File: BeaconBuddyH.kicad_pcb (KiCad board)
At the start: 2 copper layers, 25.4 x 27.9 mm, 106 parts, among them P1 CONN_01X06, U1 nRF52832-QFAA, Y1 32.768kHz, Y2 32MHz

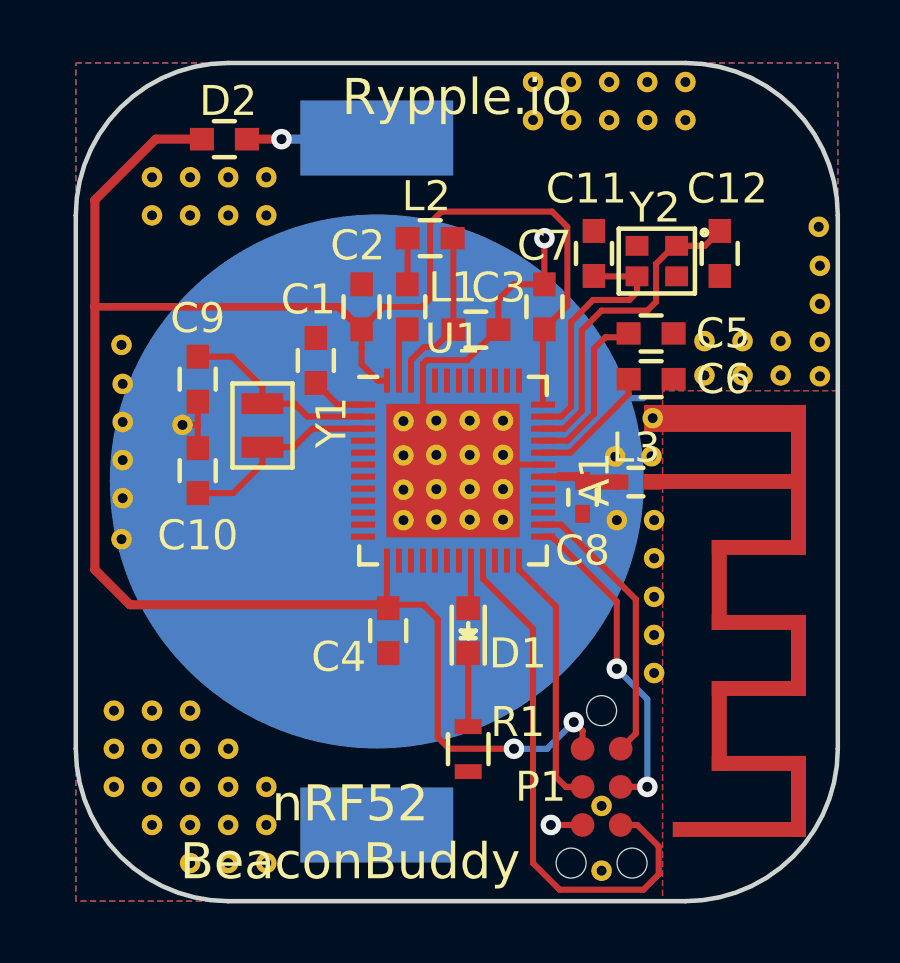
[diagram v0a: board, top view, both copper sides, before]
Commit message: Added Temp/Humidity sensor
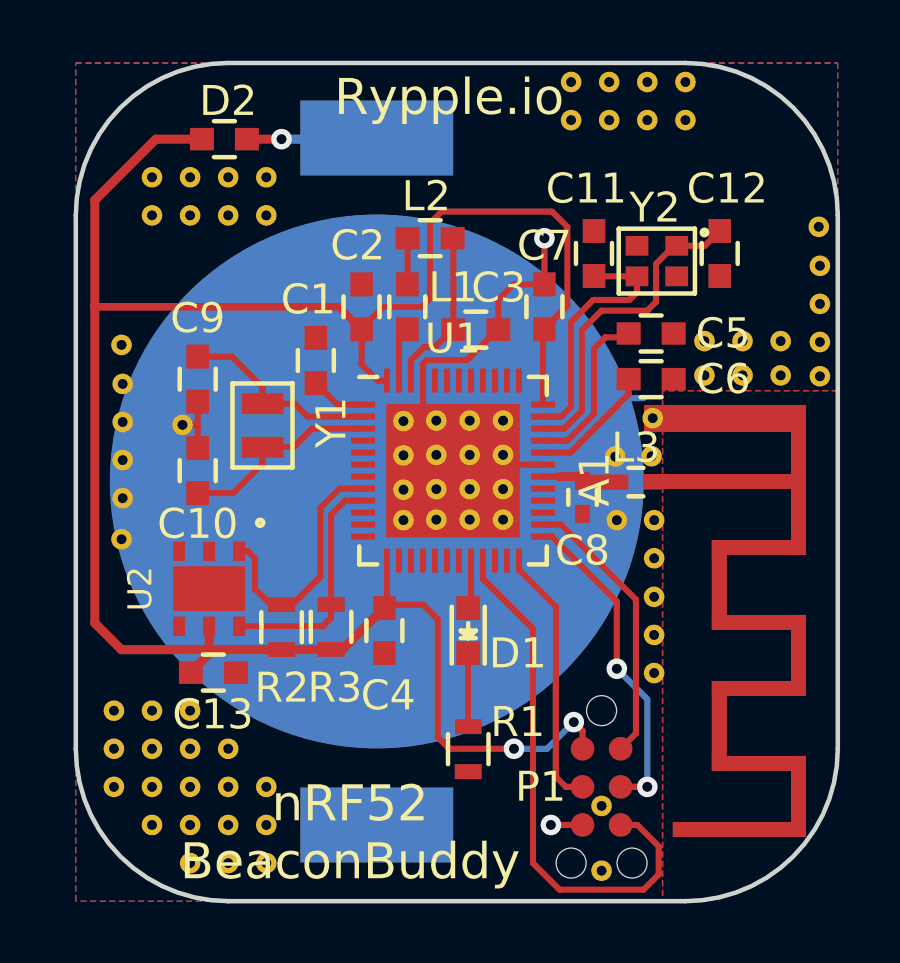
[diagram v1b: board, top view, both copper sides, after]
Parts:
- removed the REF**11 at (167.6, 102.2)
- removed the REF**12 at (167.6, 101.0)
- added C13: 0.1uF, Capacitors_SMD:C_0603, F.Cu at (157.0, 120.7)
- added R2: 470, Resistors_SMD:R_0603, F.Cu at (159.3, 119.1)
- added R3: 470, Resistors_SMD:R_0603, F.Cu at (160.9, 119.1)
- added U2: HDC1080, New_Footprints:S-PWSON-N6, F.Cu at (156.8, 117.9)
- moved C4 0.13 mm to (162.7, 119.3)
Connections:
- U1 pad 8: Net-(U1-Pad8) -> /SDA
- U1 pad 9: Net-(U1-Pad9) -> /SCL
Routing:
- net /SDA: track 0.00 -> 8.40 mm
- net /SCL: track 0.00 -> 7.88 mm
- net VDD: track 68.6 -> 73.1 mm

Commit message: Added Pressure Sensor
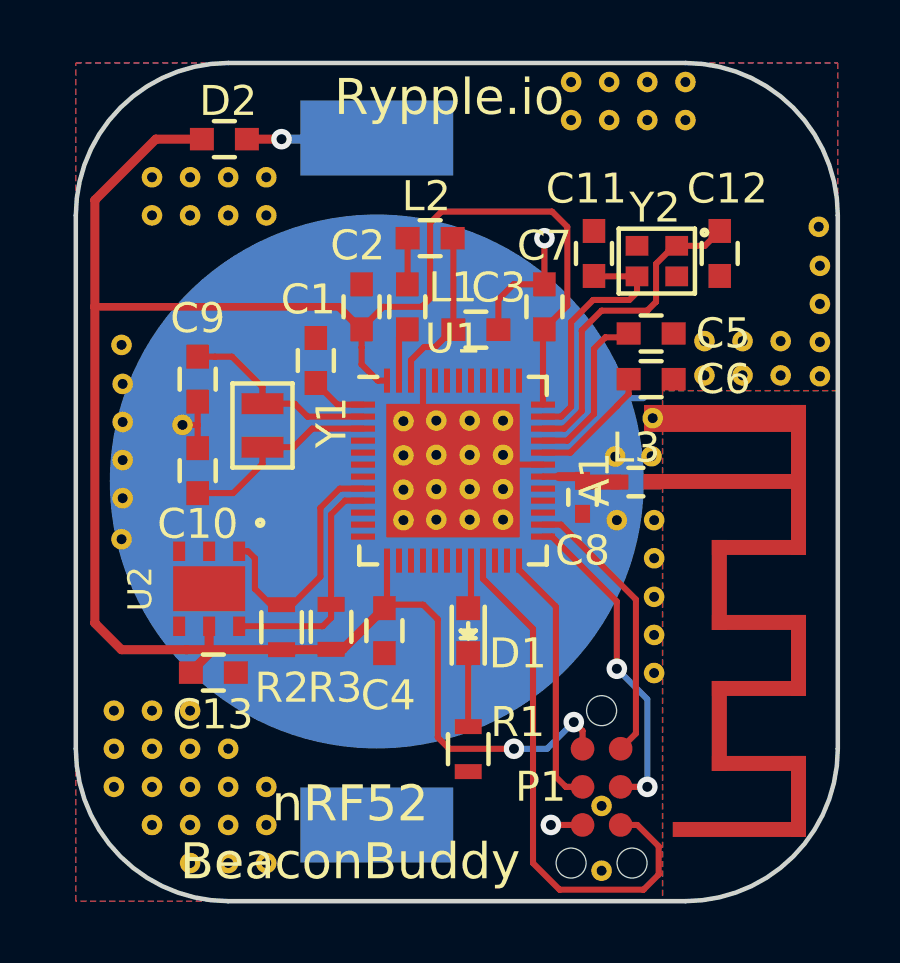
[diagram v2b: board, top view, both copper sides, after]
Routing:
- net GND: track 23.2 -> 19.7 mm
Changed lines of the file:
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@@
 (kicad_pcb (version 4) (host pcbnew 4.0.2-stable)
   (general
-    (links 172)
-    (no_connects 9)
-    (area 152.324999 100.254999 177.875001 128.345001)
+    (links 170)
+    (no_connects 2)
+    (area 149.585458 96.8396 181.432358 131.338542)
     (thickness 1.6)
     (drawings 10)
-    (tracks 210)
+    (tracks 206)
     (zones 0)
     (modules 108)
@@
   (segment (start 156.464 111.621) (end 156.464 112.395) (width 0.2032) (layer F.Cu) (net 2))
   (segment (start 156.464 112.395) (end 155.956 112.395) (width 0.2032) (layer F.Cu) (net 2))
-  (segment (start 163.973 110.919) (end 163.973 110.361798) (width 0.2032) (layer F.Cu) (net 2))
-  (segment (start 163.973 110.361798) (end 164.098798 110.236) (width 0.2032) (layer F.Cu) (net 2))
-  (segment (start 164.098798 110.236) (end 165.444 110.236) (width 0.2032) (layer F.Cu) (net 2))
   (segment (start 166.485 109.22) (end 166.46 109.22) (width 0.2032) (layer F.Cu) (net 2))
-  (segment (start 166.46 109.22) (end 165.444 110.236) (width 0.2032) (layer F.Cu) (net 2))
   (segment (start 163.957 111.506) (end 171.323 111.506) (width 0.2032) (layer B.Cu) (net 2))
   (segment (start 163.973 110.919) (end 163.973 112.919) (width 0.2032) (layer F.Cu) (net 2))

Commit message: Added optional Anemometer/Analog Input
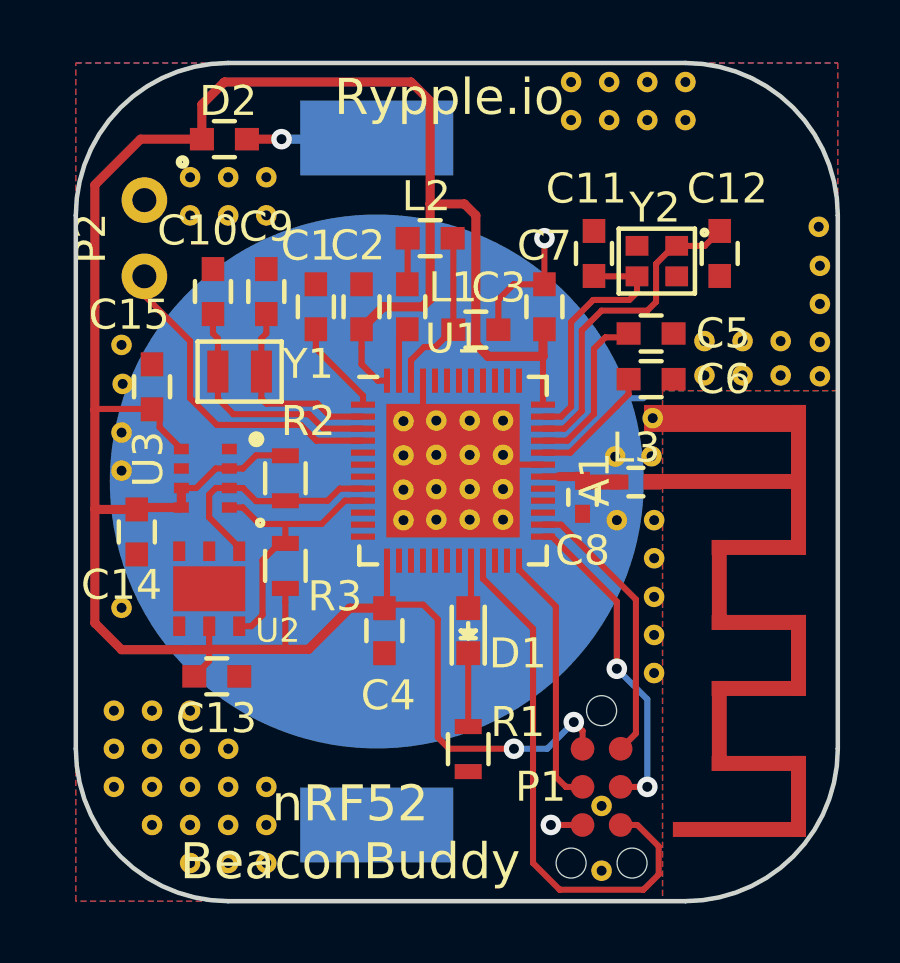
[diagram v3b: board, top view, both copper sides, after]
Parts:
- removed the REF** at (154.0, 114.8)
- removed the REF**11 at (156.0, 112.4)
- removed the REF**11 at (154.9, 105.4)
- removed the REF**12 at (154.9, 104.1)
- added C14: 0.1uF, Capacitors_SMD:C_0603, F.Cu at (154.4, 116.0)
- added C15: 0.1uF, Capacitors_SMD:C_0603, F.Cu at (154.9, 111.1)
- added P2: AIN0, New_Footprints:CONN_100mil_1x2, F.Cu at (154.7, 106.2)
- added U3: BMP280, New_Footprints:Bosch_LGA8, F.Cu at (156.7, 114.2)
- R2, R3: value 470 -> 4.7k
- U2: value HDC1080 -> Si7020-A20
- moved C10 5.99 mm to (157.0, 108.0)
- moved R2 4.97 mm to (159.4, 114.2), turned to 270 degrees
- moved C9 3.71 mm to (158.8, 108.0), turned to 270 degrees
- moved R3 2.54 mm to (159.4, 117.1)
- moved REF** 2.29 mm to (153.9, 118.5)
- moved Y1 1.95 mm to (157.9, 110.6), turned to 0 degrees
- moved C1 1.79 mm to (160.4, 108.5)
- moved REF** 0.35 mm to (153.9, 113.9)
- moved REF** 0.35 mm to (153.9, 112.6)
- moved C13 0.17 mm to (157.1, 120.8)
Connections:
- U1 pad 4: Net-(U1-Pad4) -> /AIN0
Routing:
- net VDD: track 73.1 -> 90.6 mm
- net /AIN0: track 0.00 -> 11.0 mm
- net GND: track 19.7 -> 17.6 mm
- net /SCL: track 7.88 -> 9.48 mm
- net /XL2: track 6.72 -> 8.14 mm
- net Net-(C1-Pad1): track 1.87 -> 3.16 mm

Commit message: Fixed ground pin issue:
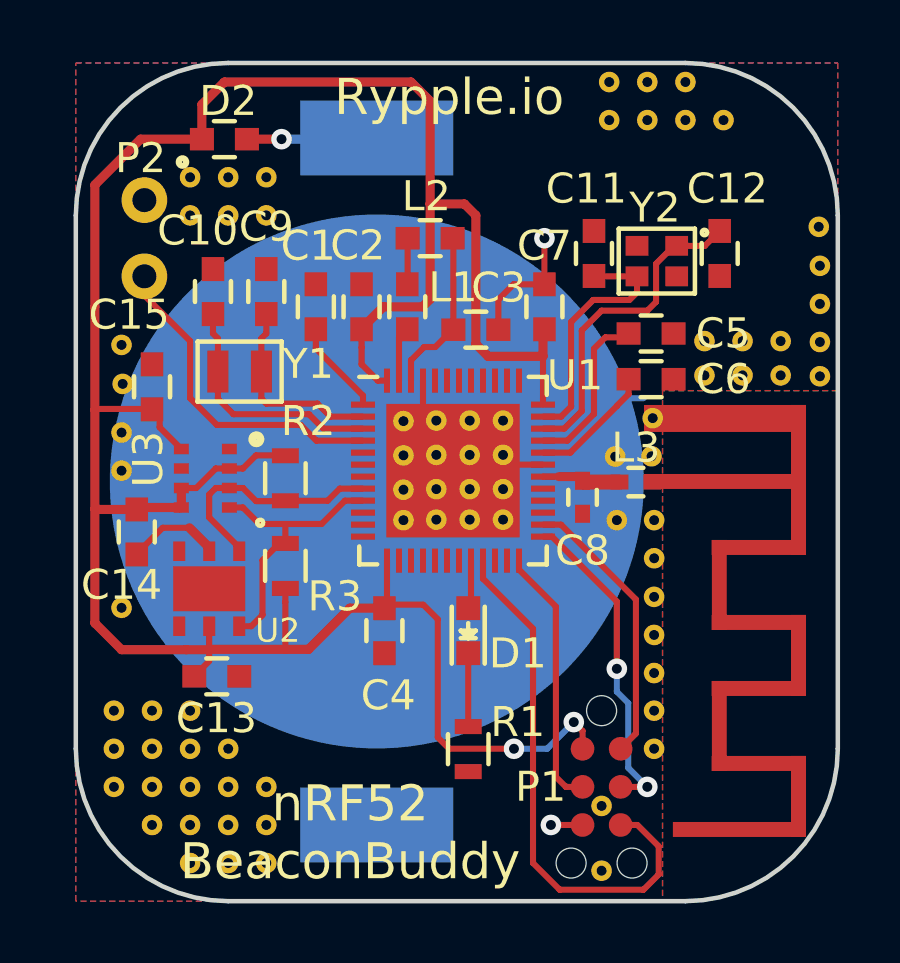
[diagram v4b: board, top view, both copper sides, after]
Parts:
- removed the REF**22 at (168.9, 101.0)
- added REF**: Via-13mil, New_Footprints:Via-13mil, F.Cu at (171.7, 123.2)
- added REF**: Via-13mil, New_Footprints:Via-13mil, F.Cu at (171.7, 121.9)
- moved REF**21 5.08 mm to (174.0, 102.2)
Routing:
- net GND: track 17.6 -> 20.8 mm
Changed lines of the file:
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@@
 (kicad_pcb (version 4) (host pcbnew 4.0.2-stable)
   (general
-    (links 180)
-    (no_connects 4)
-    (area 152.324999 100.254999 177.875001 128.345001)
+    (links 179)
+    (no_connects 1)
+    (area 149.585458 96.8396 181.432358 131.338542)
     (thickness 1.6)
     (drawings 10)
-    (tracks 252)
+    (tracks 259)
     (zones 0)
-    (modules 108)
+    (modules 109)
     (nets 52)
   )
@@
     (add_net VDD)
   )
+  (module New_Footprints:Via-13mil (layer F.Cu)
+    (at 171.676307 123.19 90)
+    (zone_connect 2)
+    (fp_text reference REF** (at 0 3.302 90) (layer F.SilkS) hide
+      (effects (font (size 1 1) (thickness 0.15)))
+    )
+    (fp_text value Via-13mil (at 0 -3.048 90) (layer F.Fab) hide
+      (effects (font (size 1 1) (thickness 0.15)))
+    )
+    (pad 1 thru_hole circle (at 0 0 90) (size 0.6858 0.6858) (drill 0.3302) (layers *.Cu)
+      (net 2 GND) (zone_connect 2))
+  )
+  (module New_Footprints:Via-13mil (layer F.Cu)
+    (at 171.676307 121.92 90)
+    (zone_connect 2)
+    (fp_text reference REF** (at 0 3.302 90) (layer F.SilkS) hide
+      (effects (font (size 1 1) (thickness 0.15)))
+    )
+    (fp_text value Via-13mil (at 0 -3.048 90) (layer F.Fab) hide
+      (effects (font (size 1 1) (thickness 0.15)))
+    )
+    (pad 1 thru_hole circle (at 0 0 90) (size 0.6858 0.6858) (drill 0.3302) (layers *.Cu)
+      (net 2 GND) (zone_connect 2))
+  )
   (module New_Footprints:Bosch_LGA8 (layer F.Cu)
     (at 156.718 114.173)
@@
   )
   (module New_Footprints:Via-13mil (layer F.Cu)
-    (at 168.91 100.965)
-    (zone_connect 2)
-    (fp_text reference REF**22 (at 0 3.302) (layer F.SilkS) hide
-      (effects (font (size 1 1) (thickness 0.15)))
-    )
-    (fp_text value Via-13mil (at 0 -3.048) (layer F.Fab) hide
-      (effects (font (size 1 1) (thickness 0.15)))
-    )
-    (pad 1 thru_hole circle (at 0 0) (size 0.6858 0.6858) (drill 0.3302) (layers *.Cu)
-      (net 2 GND) (zone_connect 2))
-  )
-  (module New_Footprints:Via-13mil (layer F.Cu)
     (at 170.18 100.965)
     (zone_connect 2)
@@
   )
   (module New_Footprints:Via-13mil (layer F.Cu)
-    (at 168.91 102.235)
+    (at 173.99 102.235)
     (zone_connect 2)
     (fp_text reference REF**21 (at 0 3.302) (layer F.SilkS) hide
@@
     (tags "QFN 0.4")
     (attr smd)
-    (fp_text reference U1 (at 0 -4.4) (layer F.SilkS)
+    (fp_text reference U1 (at 4.064 -3.175) (layer F.SilkS)
       (effects (font (size 1 1) (thickness 0.15)))
     )
@@
   (module New_Footprints:Antenna-2.45GHZ (layer F.Cu)
     (at 174.04 114.28 270)
-    (fp_text reference A1 (at -0.07 4.34 270) (layer F.SilkS)
+    (fp_text reference A1 (at -0.996 0.812 360) (layer F.SilkS) hide
       (effects (font (size 1 1) (thickness 0.15)))
     )
@@
   (module New_Footprints:CONN_100mil_1x2 (layer F.Cu)
     (at 154.686 106.172 270)
-    (fp_text reference P2 (at 0 1.778 270) (layer F.SilkS)
+    (fp_text reference P2 (at -2.667 0.127 360) (layer F.SilkS)
       (effects (font (size 1 1) (thickness 0.15)))
     )
@@
   (segment (start 160.401 109.8438) (end 160.401 109.8112) (width 0.2032) (layer F.Cu) (net 1))
   (segment (start 160.401 109.8112) (end 160.401 109.208) (width 0.2032) (layer F.Cu) (net 1))
+  (segment (start 156.188 115.824) (end 155.296 115.824) (width 0.2032) (layer F.Cu) (net 2))
+  (segment (start 155.296 115.824) (end 154.432 116.688) (width 0.2032) (layer F.Cu) (net 2))
+  (segment (start 154.432 116.688) (end 154.432 116.713) (width 0.2032) (layer F.Cu) (net 2))
+  (segment (start 156.845 116.606) (end 156.845 116.481) (width 0.2032) (layer F.Cu) (net 2))
+  (segment (start 156.845 116.481) (end 156.188 115.824) (width 0.3048) (layer F.Cu) (net 2))
   (via (at 168.23692 125.73) (size 0.6858) (drill 0.3302) (layers F.Cu B.Cu) (net 2))
   (segment (start 169.291 125.73) (end 168.23692 125.73) (width 0.2032) (layer F.Cu) (net 2))
@@
   (segment (start 168.402 118.448) (end 167.173 117.219) (width 0.2032) (layer F.Cu) (net 29))
   (segment (start 167.173 117.219) (end 167.173 116.919) (width 0.2032) (layer F.Cu) (net 29))
-  (segment (start 171.45 124.46) (end 171.45 121.539) (width 0.2032) (layer B.Cu) (net 30))
-  (segment (start 171.45 121.539) (end 170.434 120.523) (width 0.2032) (layer B.Cu) (net 30))
+  (segment (start 171.45 124.46) (end 170.815 123.825) (width 0.2032) (layer B.Cu) (net 30))
+  (segment (start 170.815 123.825) (end 170.815 121.666) (width 0.2032) (layer B.Cu) (net 30))
+  (segment (start 170.815 121.666) (end 170.434 121.285) (width 0.2032) (layer B.Cu) (net 30))
+  (segment (start 170.434 121.285) (end 170.434 120.523) (width 0.2032) (layer B.Cu) (net 30))
   (via (at 170.434 120.523) (size 0.6858) (drill 0.3302) (layers F.Cu B.Cu) (net 30))
   (segment (start 167.973 116.119) (end 168.273 116.119) (width 0.2032) (layer F.Cu) (net 30))
